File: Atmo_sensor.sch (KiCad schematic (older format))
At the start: 4 parts

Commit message: Fix atmo sensor, add LoRa schematic
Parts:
- removed R? (x2): 4k7, symbol Device:R
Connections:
- wire segments 22 -> 18
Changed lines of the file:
@@
-	1    0    0    -1
-$EndComp
-$Comp
-L Device:R R?
-U 1 1 60A54F5B
-P 5900 3050
-F 0 "R?" H 5830 3096 50  0000 R CNN
-F 1 "4k7" H 5830 3005 50  0000 R CNN
-F 2 "" V 5830 3050 50  0001 C CNN
-F 3 "~" H 5900 3050 50  0001 C CNN
-	1    5900 3050
-	1    0    0    -1
-$EndComp
-$Comp
-L Device:R R?
-U 1 1 60A558B2
-P 6100 3050
-F 0 "R?" H 6170 3096 50  0000 L CNN
-F 1 "4k7" H 6170 3005 50  0000 L CNN
-F 2 "" V 6030 3050 50  0001 C CNN
-F 3 "~" H 6100 3050 50  0001 C CNN
-	1    6100 3050
 	1    0    0    -1
 $EndComp
@@
 Wire Wire Line
 	5600 3100 5500 3100
-Wire Wire Line
-	5600 3100 5600 2800
-Wire Wire Line
-	5600 2800 5600 2700
 Connection ~ 5600 3100
-Wire Wire Line
-	6100 2800 6100 2900
-Wire Wire Line
-	5900 2900 5900 2800
-Wire Wire Line
-	5900 3200 5900 3300
-Connection ~ 5600 2800
-Connection ~ 5900 2800
-Wire Wire Line
-	5900 2800 6100 2800
-Wire Wire Line
-	5600 2800 5900 2800
-Connection ~ 5900 3300
-Wire Wire Line
-	5500 3300 5900 3300
-Wire Wire Line
-	6100 3200 6100 3500
-Wire Wire Line
-	5500 3500 6100 3500
-Connection ~ 6100 3500
-Wire Wire Line
-	6100 3500 6200 3500
-Wire Wire Line
-	5900 3300 6200 3300
 Text Notes 5650 3650 0    50   ~ 0
 I2C Addr: 1110111
+Wire Wire Line
+	5500 3300 6200 3300
+Wire Wire Line
+	5500 3500 6200 3500
+Wire Wire Line
+	5600 2700 5600 3100
+$Comp
+L power:GND #PWR?
+U 1 1 60A536E3
+P 4900 4100
+F 0 "#PWR?" H 4900 3850 50  0001 C CNN
+F 1 "GND" H 4905 3927 50  0000 C CNN
+F 2 "" H 4900 4100 50  0001 C CNN
+F 3 "" H 4900 4100 50  0001 C CNN
+	1    4900 4100
+	1    0    0    -1
+$EndComp
+Wire Wire Line
+	4800 4000 4800 4050
+Wire Wire Line
+	5000 4000 5000 4050
+Wire Wire Line
+	5000 4050 4900 4050
+Wire Wire Line
+	4900 4050 4900 4100
+Connection ~ 4900 4050
+Wire Wire Line
+	4900 4050 4800 4050
 $EndSCHEMATC

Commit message: Change BME280 out for connector
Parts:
- removed C?: 0.1uF, symbol Device:C
- removed U?: BME280, Package_LGA:Bosch_LGA-8_2.5x2.5mm_P0.65mm_ClockwisePinNumbering, symbol Sensor:BME280
- added J?: 100mil hdr, symbol Connector:Conn_01x04_Female
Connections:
- wire segments 18 -> 6
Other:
- note added: "I2C Addr: 1110110\non GYBMEP board"
- note removed: "I2C Addr: 1110111"
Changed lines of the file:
@@
 Comment4 ""
 $EndDescr
+Text HLabel 6100 4000 2    50   BiDi ~ 0
+SDA
+Text HLabel 6100 3900 2    50   BiDi ~ 0
+SCL
+Text Notes 5000 4200 0    50   ~ 0
+I2C Addr: 1110110\non GYBMEP board
 $Comp
-L Sensor:BME280 U?
-U 1 1 60A4E35E
-P 4900 3400
-F 0 "U?" H 4471 3446 50  0000 R CNN
-F 1 "BME280" H 4471 3355 50  0000 R CNN
-F 2 "Package_LGA:Bosch_LGA-8_2.5x2.5mm_P0.65mm_ClockwisePinNumbering" H 6400 2950 50  0001 C CNN
-F 3 "https://ae-bst.resource.bosch.com/media/_tech/media/datasheets/BST-BME280-DS002.pdf" H 4900 3200 50  0001 C CNN
-	1    4900 3400
-	1    0    0    -1
+L Connector:Conn_01x04_Female J?
+U 1 1 60AAC14B
+P 5600 3900
+F 0 "J?" H 5492 3475 50  0000 C CNN
+F 1 "100mil hdr" H 5492 3566 50  0000 C CNN
+F 2 "" H 5600 3900 50  0001 C CNN
+F 3 "~" H 5600 3900 50  0001 C CNN
+	1    5600 3900
+	-1   0    0    1
 $EndComp
+Wire Wire Line
+	6000 3800 5800 3800
+Wire Wire Line
+	6000 3800 6000 4100
+Wire Wire Line
+	5800 3700 6000 3700
+Wire Wire Line
+	6000 3700 6000 3500
+Wire Wire Line
+	5800 3900 6100 3900
+Wire Wire Line
+	5800 4000 6100 4000
 $Comp
 L power:+3V3 #PWR?
-U 1 1 60A4EFA1
-P 4400 2200
-F 0 "#PWR?" H 4400 2050 50  0001 C CNN
-F 1 "+3V3" H 4415 2373 50  0000 C CNN
-F 2 "" H 4400 2200 50  0001 C CNN
-F 3 "" H 4400 2200 50  0001 C CNN
-	1    4400 2200
-	1    0    0    -1
-$EndComp
-$Comp
-L Device:C C?
-U 1 1 60A4FF45
-P 4400 2450
-F 0 "C?" H 4515 2496 50  0000 L CNN
-F 1 "0.1uF" H 4515 2405 50  0000 L CNN
-F 2 "" H 4438 2300 50  0001 C CNN
-F 3 "~" H 4400 2450 50  0001 C CNN
-	1    4400 2450
+U 1 1 60AAF65C
+P 6000 3500
+F 0 "#PWR?" H 6000 3350 50  0001 C CNN
+F 1 "+3V3" H 6015 3673 50  0000 C CNN
+F 2 "" H 6000 3500 50  0001 C CNN
+F 3 "" H 6000 3500 50  0001 C CNN
+	1    6000 3500
 	1    0    0    -1
 $EndComp
 $Comp
 L power:GND #PWR?
-U 1 1 60A50DFF
-P 4400 2700
-F 0 "#PWR?" H 4400 2450 50  0001 C CNN
-F 1 "GND" H 4405 2527 50  0000 C CNN
-F 2 "" H 4400 2700 50  0001 C CNN
-F 3 "" H 4400 2700 50  0001 C CNN
-	1    4400 2700
+U 1 1 60AAF99E
+P 6000 4100
+F 0 "#PWR?" H 6000 3850 50  0001 C CNN
+F 1 "GND" H 6005 3927 50  0000 C CNN
+F 2 "" H 6000 4100 50  0001 C CNN
+F 3 "" H 6000 4100 50  0001 C CNN
+	1    6000 4100
 	1    0    0    -1
 $EndComp
-Wire Wire Line
-	4400 2700 4400 2600
-Wire Wire Line
-	4400 2300 4400 2200
-Wire Wire Line
-	4800 2300 4800 2700
-Wire Wire Line
-	5000 2800 5000 2700
-Wire Wire Line
-	5000 2700 4800 2700
-Connection ~ 4800 2700
-Wire Wire Line
-	4800 2700 4800 2800
-Wire Wire Line
-	4400 2300 4800 2300
-Connection ~ 4400 2300
-Text HLabel 6200 3500 2    50   BiDi ~ 0
-SDA
-Text HLabel 6200 3300 2    50   BiDi ~ 0
-SCL
-$Comp
-L power:+3V3 #PWR?
-U 1 1 60A53583
-P 5600 2700
-F 0 "#PWR?" H 5600 2550 50  0001 C CNN
-F 1 "+3V3" H 5615 2873 50  0000 C CNN
-F 2 "" H 5600 2700 50  0001 C CNN
-F 3 "" H 5600 2700 50  0001 C CNN
-	1    5600 2700
-	1    0    0    -1
-$EndComp
-Wire Wire Line
-	5500 3700 5600 3700
-Wire Wire Line
-	5600 3700 5600 3100
-Wire Wire Line
-	5600 3100 5500 3100
-Connection ~ 5600 3100
-Text Notes 5650 3650 0    50   ~ 0
-I2C Addr: 1110111
-Wire Wire Line
-	5500 3300 6200 3300
-Wire Wire Line
-	5500 3500 6200 3500
-Wire Wire Line
-	5600 2700 5600 3100
-$Comp
-L power:GND #PWR?
-U 1 1 60A536E3
-P 4900 4100
-F 0 "#PWR?" H 4900 3850 50  0001 C CNN
-F 1 "GND" H 4905 3927 50  0000 C CNN
-F 2 "" H 4900 4100 50  0001 C CNN
-F 3 "" H 4900 4100 50  0001 C CNN
-	1    4900 4100
-	1    0    0    -1
-$EndComp
-Wire Wire Line
-	4800 4000 4800 4050
-Wire Wire Line
-	5000 4000 5000 4050
-Wire Wire Line
-	5000 4050 4900 4050
-Wire Wire Line
-	4900 4050 4900 4100
-Connection ~ 4900 4050
-Wire Wire Line
-	4900 4050 4800 4050
 $EndSCHEMATC

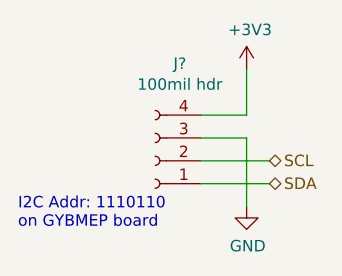
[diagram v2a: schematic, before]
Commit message: Begin assigning footprints
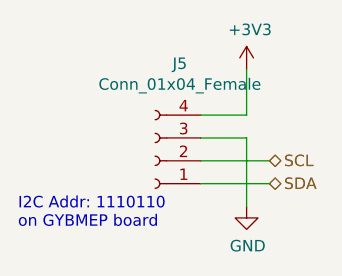
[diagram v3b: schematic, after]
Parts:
- J5: renamed from J?; value 100mil hdr -> Conn_01x04_Female; footprint (none) -> Connector_PinSocket_2.54mm:PinSocket_1x04_P2.54mm_Vertical
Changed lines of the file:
@@
 I2C Addr: 1110110\non GYBMEP board
 $Comp
-L Connector:Conn_01x04_Female J?
+L Connector:Conn_01x04_Female J5
 U 1 1 60AAC14B
 P 5600 3900
-F 0 "J?" H 5492 3475 50  0000 C CNN
-F 1 "100mil hdr" H 5492 3566 50  0000 C CNN
-F 2 "" H 5600 3900 50  0001 C CNN
+F 0 "J5" H 5492 3475 50  0000 C CNN
+F 1 "Conn_01x04_Female" H 5492 3566 50  0000 C CNN
+F 2 "Connector_PinSocket_2.54mm:PinSocket_1x04_P2.54mm_Vertical" H 5600 3900 50  0001 C CNN
 F 3 "~" H 5600 3900 50  0001 C CNN
 	1    5600 3900
@@
 	5800 4000 6100 4000
 $Comp
-L power:+3V3 #PWR?
+L power:+3V3 #PWR011
 U 1 1 60AAF65C
 P 6000 3500
-F 0 "#PWR?" H 6000 3350 50  0001 C CNN
+F 0 "#PWR011" H 6000 3350 50  0001 C CNN
 F 1 "+3V3" H 6015 3673 50  0000 C CNN
 F 2 "" H 6000 3500 50  0001 C CNN
@@
 $EndComp
 $Comp
-L power:GND #PWR?
+L power:GND #PWR012
 U 1 1 60AAF99E
 P 6000 4100
-F 0 "#PWR?" H 6000 3850 50  0001 C CNN
+F 0 "#PWR012" H 6000 3850 50  0001 C CNN
 F 1 "GND" H 6005 3927 50  0000 C CNN
 F 2 "" H 6000 4100 50  0001 C CNN

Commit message: Finalize schematic
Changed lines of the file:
@@
 Text HLabel 6100 3900 2    50   BiDi ~ 0
 SCL
-Text Notes 5000 4200 0    50   ~ 0
+Text Notes 5000 4600 0    50   ~ 0
 I2C Addr: 1110110\non GYBMEP board
 $Comp

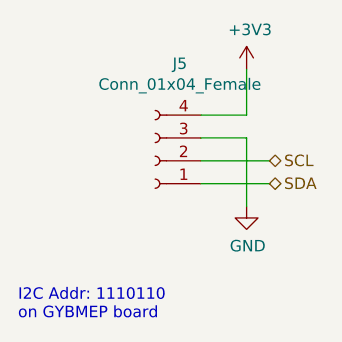
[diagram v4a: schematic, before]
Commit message: Finish routing of Rev 1
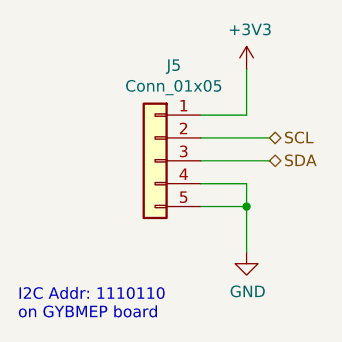
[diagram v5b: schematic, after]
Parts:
- removed J5: Conn_01x04_Female, Connector_PinSocket_2.54mm:PinSocket_1x04_P2.54mm_Vertical, symbol Connector:Conn_01x04_Female
- added J5: Conn_01x05, Connector_JST:JST_XH_B5B-XH-AM_1x05_P2.50mm_Vertical, symbol Connector_Generic:Conn_01x05
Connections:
- net +3V3: now also J5.1 (Pin_1)
- net GND: now also J5.4 (Pin_4), J5.5 (Pin_5)
- net SCL: now also J5.2 (Pin_2)
- net SDA: now also J5.3 (Pin_3)
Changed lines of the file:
@@
 $Descr A4 11693 8268
 encoding utf-8
-Sheet 4 9
+Sheet 4 10
 Title ""
 Date ""
@@
 Comment4 ""
 $EndDescr
-Text HLabel 6100 4000 2    50   BiDi ~ 0
+Text HLabel 6100 3900 2    50   BiDi ~ 0
 SDA
-Text HLabel 6100 3900 2    50   BiDi ~ 0
+Text HLabel 6100 3800 2    50   BiDi ~ 0
 SCL
 Text Notes 5000 4600 0    50   ~ 0
 I2C Addr: 1110110\non GYBMEP board
-$Comp
-L Connector:Conn_01x04_Female J5
-U 1 1 60AAC14B
-P 5600 3900
-F 0 "J5" H 5492 3475 50  0000 C CNN
-F 1 "Conn_01x04_Female" H 5492 3566 50  0000 C CNN
-F 2 "Connector_PinSocket_2.54mm:PinSocket_1x04_P2.54mm_Vertical" H 5600 3900 50  0001 C CNN
-F 3 "~" H 5600 3900 50  0001 C CNN
-	1    5600 3900
-	-1   0    0    1
-$EndComp
 Wire Wire Line
-	6000 3800 5800 3800
+	6000 4000 5800 4000
 Wire Wire Line
-	6000 3800 6000 4100
+	6000 4000 6000 4100
 Wire Wire Line
 	5800 3700 6000 3700
@@
 	6000 3700 6000 3500
 Wire Wire Line
+	5800 3800 6100 3800
+Wire Wire Line
 	5800 3900 6100 3900
-Wire Wire Line
-	5800 4000 6100 4000
 $Comp
 L power:+3V3 #PWR011
@@
 L power:GND #PWR012
 U 1 1 60AAF99E
-P 6000 4100
-F 0 "#PWR012" H 6000 3850 50  0001 C CNN
-F 1 "GND" H 6005 3927 50  0000 C CNN
-F 2 "" H 6000 4100 50  0001 C CNN
-F 3 "" H 6000 4100 50  0001 C CNN
-	1    6000 4100
+P 6000 4300
+F 0 "#PWR012" H 6000 4050 50  0001 C CNN
+F 1 "GND" H 6005 4127 50  0000 C CNN
+F 2 "" H 6000 4300 50  0001 C CNN
+F 3 "" H 6000 4300 50  0001 C CNN
+	1    6000 4300
 	1    0    0    -1
 $EndComp
+$Comp
+L Connector_Generic:Conn_01x05 J?
+U 1 1 60D6AB27
+P 5600 3900
+AR Path="/60A49A7C/60D6AB27" Ref="J?"  Part="1"
+AR Path="/60A4AC4A/60D6AB27" Ref="J?"  Part="1"
+AR Path="/60A4FAC1/60D6AB27" Ref="J5"  Part="1"
+F 0 "J5" H 5518 4317 50  0000 C CNN
+F 1 "Conn_01x05" H 5518 4226 50  0000 C CNN
+F 2 "Connector_JST:JST_XH_B5B-XH-AM_1x05_P2.50mm_Vertical" H 5600 3900 50  0001 C CNN
+F 3 "~" H 5600 3900 50  0001 C CNN
+	1    5600 3900
+	-1   0    0    -1
+$EndComp
+Wire Wire Line
+	5800 4100 6000 4100
+Connection ~ 6000 4100
+Wire Wire Line
+	6000 4100 6000 4300
 $EndSCHEMATC
